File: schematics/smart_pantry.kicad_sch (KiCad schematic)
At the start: 5 parts, among them J1 Raspberry_Pi_4, U1 HC-SR04, U2 LM2596, U3 SSD1306, U4 WS2812E

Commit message: Updated KiCAD Schematic
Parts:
- added R1: 1k, symbol Device:R_US
- added R2: 2k, symbol Device:R_US
- added R3: 330, symbol Device:R_US
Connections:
- net +12V_IN: now reaches U2.1 (IN+)
- net GND: now reaches U2.2 (IN-)
- net GND: now also J1.14 (GND), J1.20 (GND), J1.25 (GND), J1.30 (GND), J1.34 (GND), J1.39 (GND), J1.6 (GND), J1.9 (GND), U1.4 (GND), U2.3 (OUT-), U3.4 (GND), U4.3 (GND), R2.1
- net +5V_RAIL: now reaches U2.4 (OUT+)
- net +5V_RAIL: now also J1.2 (5V), J1.4 (5V), U1.1 (VCC), U4.1 (+5V)
- net at U3.1 (VCC): now also J1.1 (3V3), J1.17 (3V3)
- net at U3.2 (SCL): now also J1.3 (SDA_I2C1/GPIO02)
- net at U3.3 (SDA): now also J1.5 (SCL_I2C1/GPIO03)
- net at J1.12 (GPIO18/SPI1_~{CE0}/PCM_CLK/PWM0): now also R3.2
- net at J1.16 (GPIO23/SDIO_CMD): now also U1.2 (TRIG)
- net at J1.18 (GPIO24/SDIO_DAT0): now also R1.2, R2.2
- net at U1.3 (ECHO): now also R1.1
- net at U4.2 (Din): now also R3.1
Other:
- moved on the sheet: J1, U1, U2, U3, U4

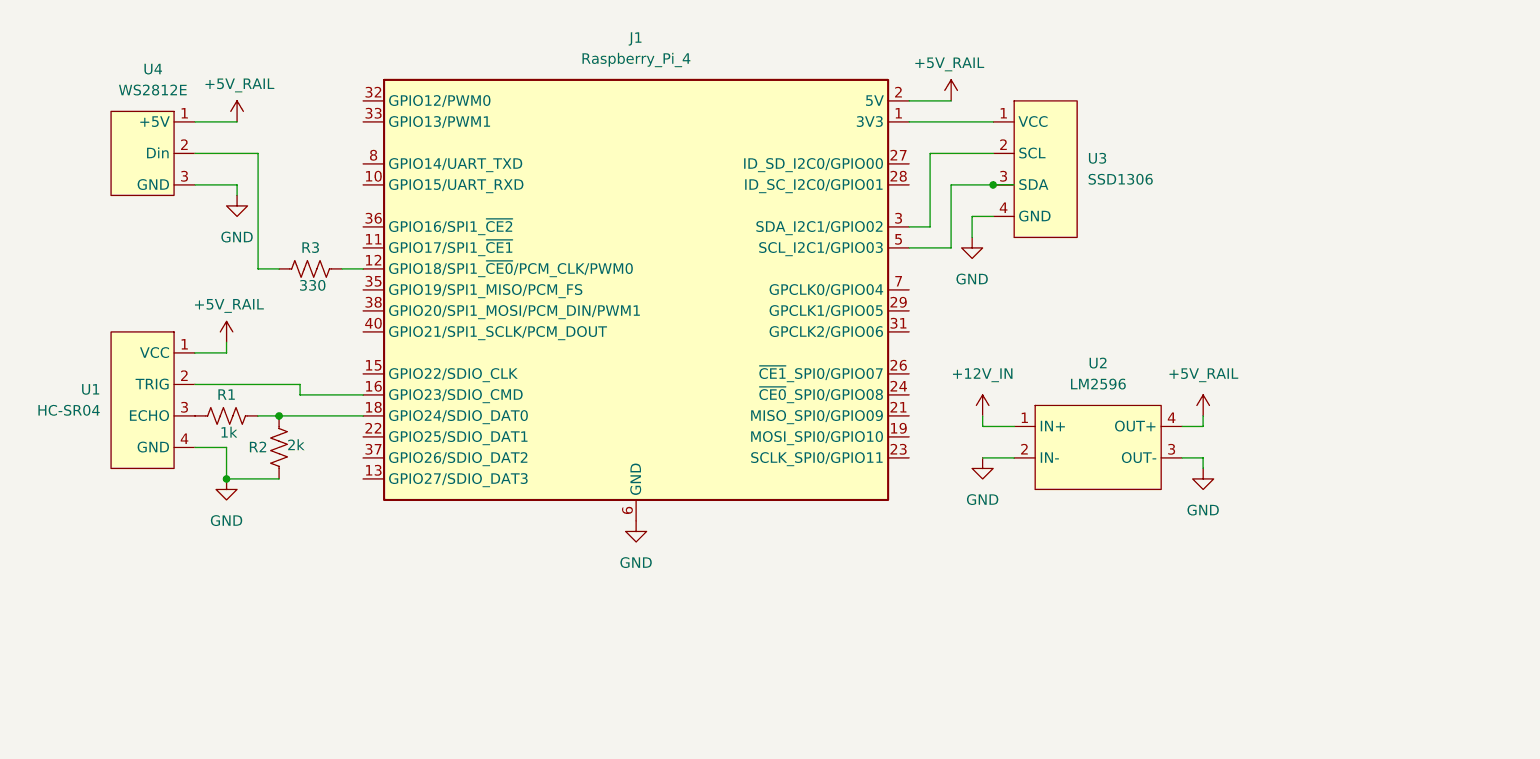
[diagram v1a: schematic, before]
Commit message: Updated KiCAD schematic & symbols to reflect ESP32 usage
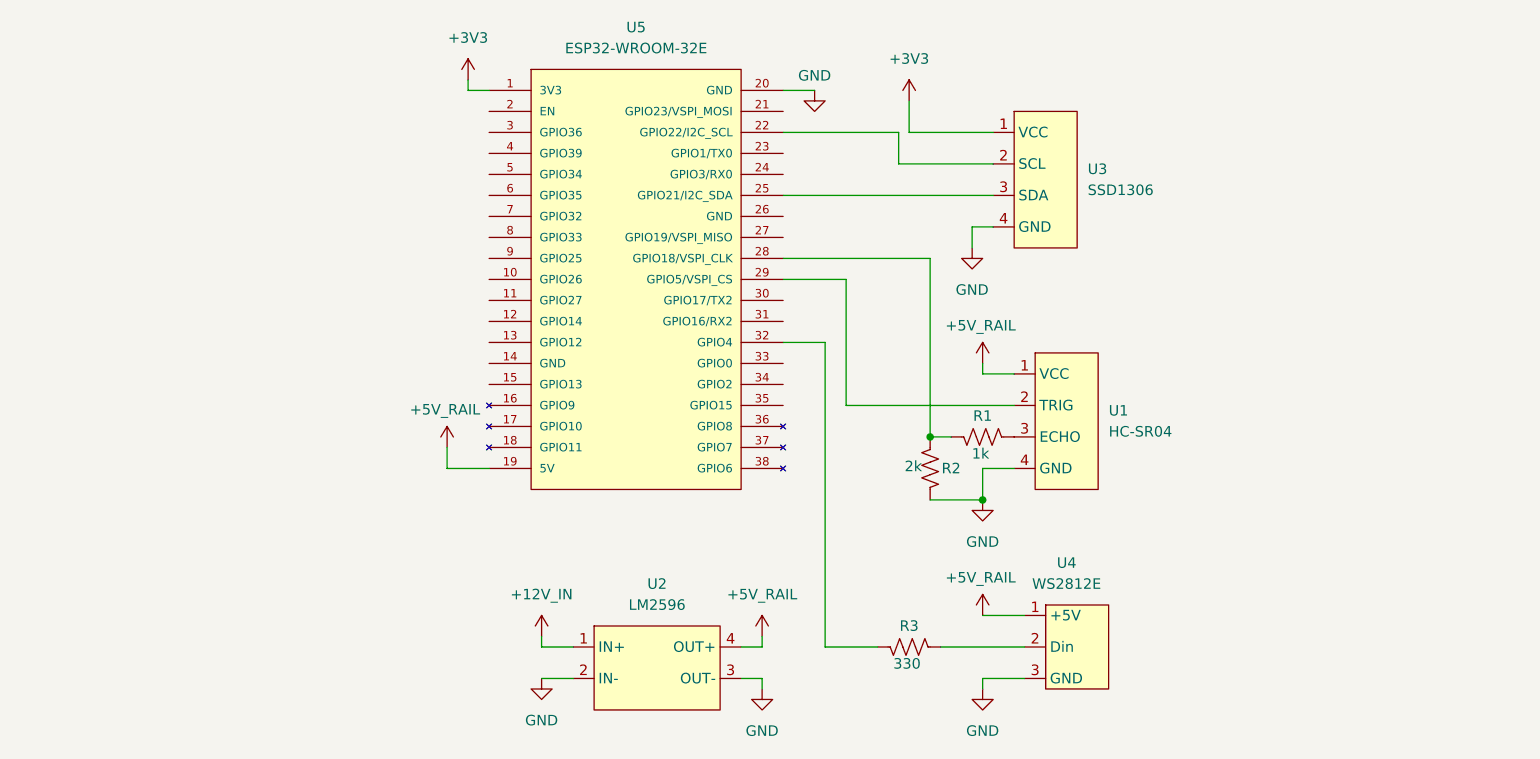
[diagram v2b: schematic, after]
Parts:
- removed J1: Raspberry_Pi_4, symbol Connector:Raspberry_Pi_4
- added U5: ESP32-WROOM-32E, RF_Module:ESP32-WROOM-32, symbol smart_pantry_symbols:ESP32-WROOM-32E
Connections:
- net +5V_RAIL: now also U5.19 (5V)
- net GND: now also U5.20 (GND)
- net at R1.2, R2.2: now also U5.28 (GPIO18/VSPI_CLK)
- net +3V3: now reaches U3.1 (VCC)
- net +3V3: now also U5.1 (3V3)
- net at U3.2 (SCL): now also U5.22 (GPIO22/I2C_SCL)
- net at U3.3 (SDA): now also U5.25 (GPIO21/I2C_SDA)
- net at R3.2: now also U5.32 (GPIO4)
- net at U1.2 (TRIG): now also U5.29 (GPIO5/VSPI_CS)
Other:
- moved on the sheet: R1, R2, R3, U1, U2, U3, U4
